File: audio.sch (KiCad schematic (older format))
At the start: 0 parts

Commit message: Add LM386 amp circuits and hierarchy pins.
Add two LM386 amplifier circuit schematics to audio subsystem.
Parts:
- added C? (x2): 100 uF, symbol Device:CP1
- added C? (x6): 0.1 uF, symbol Device:C
- added C? (x2): 1000 uF, symbol Device:CP1
- added C? (x2): 10 uF, symbol Device:CP1
- added C? (x2): 470 pF, symbol Device:C
- added LS? (x2): Speaker, symbol Device:Speaker
- added R? (x2): 10 ohm, symbol Device:R
- added R? (x2): 10k ohm, symbol Device:R
- added RV? (x2): 10k, symbol Device:R_POT_TRIM_US
- added U6, U?: LM386, symbol Amplifier_Audio:LM386
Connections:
- new net: RV?.2, U6.3 (+)
- new net: C?.1, C?.2, U6.5
- new net: R?.1, U6.7 (BYPASS)
- new net: C?.2, LS?.1 (x2)
- new net: C?.1, R?.1 (x2)
- new net: C?.1, R?.2 (x2)
- new net: RV?.2, U?.3 (+)
- new net: C?.1, C?.2, U?.5
- new net: R?.1, U?.7 (BYPASS)
- new net audio-gnd: C?.1, C?.1, C?.1, C?.1, C?.1, C?.1, C?.1, C?.1, C?.2, C?.2, C?.2, C?.2, C?.2, C?.2, C?.2, C?.2, C?.2, C?.2, LS?.2, LS?.2, R?.2, R?.2, RV?.3, RV?.3, U6.2 (-), U6.4 (GND), U6.6 (V+), U?.2 (-), U?.4 (GND), U?.6 (V+)
- new net audio-in-left: RV?.1
- new net audio-in-right: RV?.1
- no-connect marks 0 -> 4

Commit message: Implement Adafruit I2S stereo decoder symbol.
Add stereo decoder to audio subsystem schematic. NOTE: the adafruit
library may be separated out later if necessary. Change hierarchical
schematic pins coming in/out of the audio subsystem.
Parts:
- added U?: UDA1334A, symbol adafruit:UDA1334A
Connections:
- net labels added: agnd, audio-bclk, audio-channel-select, audio-in, bclk, din, wsel
- net labels removed: audio-in-left, audio-in-right
- wire segments 80 -> 91
- no-connect marks 4 -> 11
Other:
- note added: "MUTE might\nbe useful later\nfor software mute"
- moved on the sheet: C?, LS?, R?, RV?, U6, U?

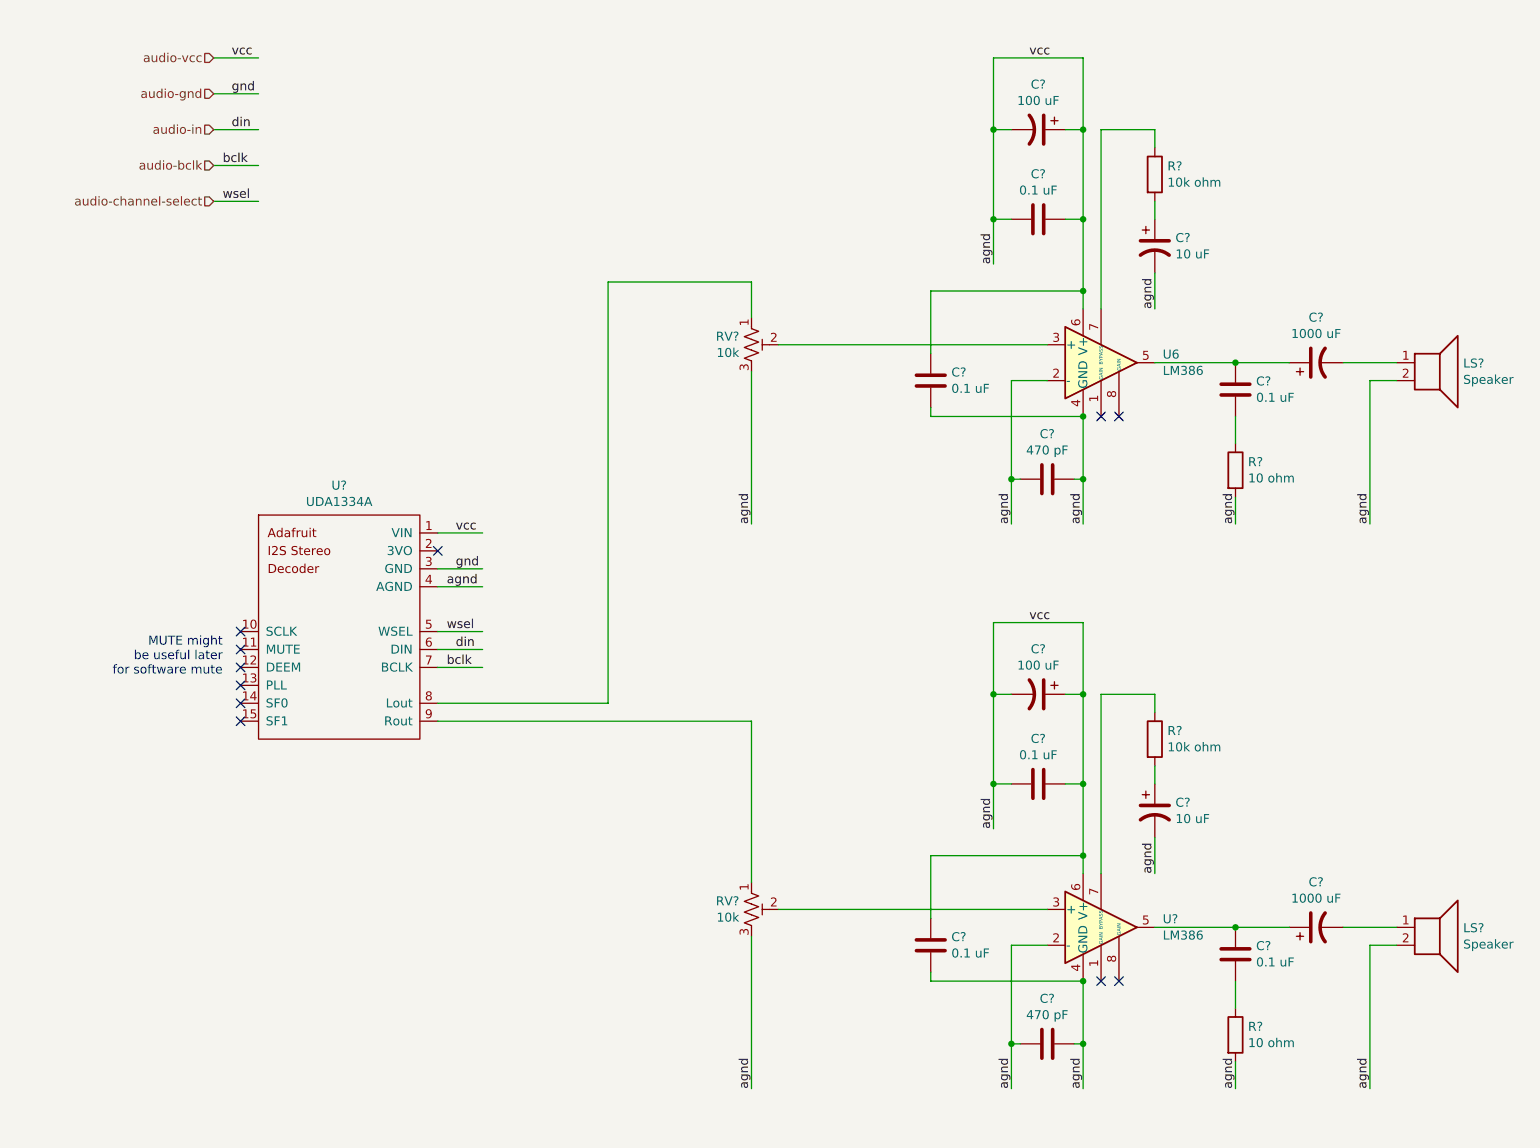
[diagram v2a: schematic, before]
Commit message: Fix power pins to remove ERC warnings.
Add global VCC and GND power pins. Add PWR_FLAG to Arduino VCC and to
audio subsystem power pins to remove ERC warnings.

Add Not Connected to all applicable pins.
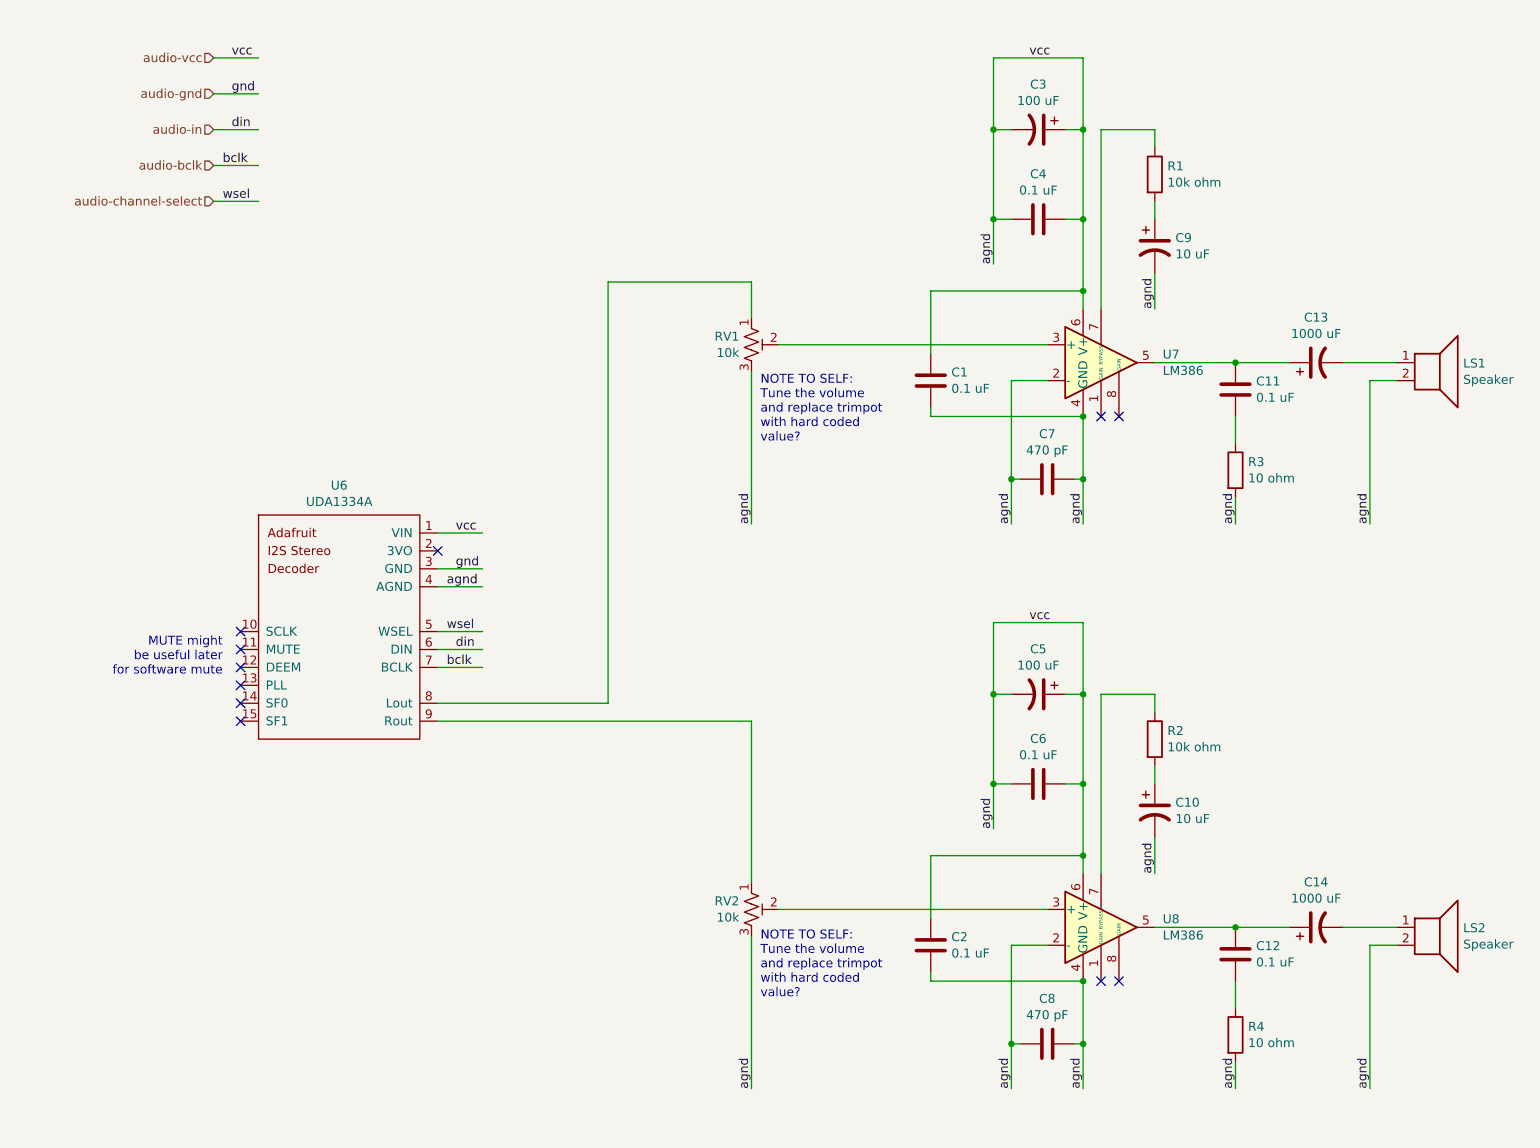
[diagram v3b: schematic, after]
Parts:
- gave numbers to parts that had none: 24
- renumbered U6 to U7
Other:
- note added: "NOTE TO SELF:\nTune the volume\nand replace trimpot\nwith hard coded\nvalue?"
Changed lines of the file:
@@
 $EndDescr
 $Comp
-L Amplifier_Audio:LM386 U6
+L Amplifier_Audio:LM386 U7
 U 1 1 60687AB3
 P 6700 2500
-F 0 "U6" H 7044 2546 50  0000 L CNN
+F 0 "U7" H 7044 2546 50  0000 L CNN
 F 1 "LM386" H 7044 2455 50  0000 L CNN
 F 2 "" H 6800 2600 50  0001 C CNN
@@
 $EndComp
 $Comp
-L Device:Speaker LS?
+L Device:Speaker LS1
 U 1 1 606892D7
 P 8550 2500
-F 0 "LS?" H 8720 2496 50  0000 L CNN
+F 0 "LS1" H 8720 2496 50  0000 L CNN
 F 1 "Speaker" H 8720 2405 50  0000 L CNN
 F 2 "" H 8550 2300 50  0001 C CNN
@@
 agnd
 $Comp
-L Device:C C?
+L Device:C C4
 U 1 1 6068C1D2
 P 6350 1700
-F 0 "C?" V 6098 1700 50  0000 C CNN
+F 0 "C4" V 6098 1700 50  0000 C CNN
 F 1 "0.1 uF" V 6189 1700 50  0000 C CNN
 F 2 "" H 6388 1550 50  0001 C CNN
@@
 $EndComp
 $Comp
-L Device:CP1 C?
+L Device:CP1 C3
 U 1 1 6068BB5D
 P 6350 1200
-F 0 "C?" V 6098 1200 50  0000 C CNN
+F 0 "C3" V 6098 1200 50  0000 C CNN
 F 1 "100 uF" V 6189 1200 50  0000 C CNN
 F 2 "" H 6350 1200 50  0001 C CNN
@@
 NoConn ~ 6800 2800
 $Comp
-L Device:C C?
+L Device:C C11
 U 1 1 6069163A
 P 7450 2650
-F 0 "C?" H 7335 2604 50  0000 R CNN
+F 0 "C11" H 7335 2604 50  0000 R CNN
 F 1 "0.1 uF" H 7335 2695 50  0000 R CNN
 F 2 "" H 7488 2500 50  0001 C CNN
@@
 $EndComp
 $Comp
-L Device:R R?
+L Device:R R3
 U 1 1 60692BCE
 P 7450 3100
-F 0 "R?" H 7520 3146 50  0000 L CNN
+F 0 "R3" H 7520 3146 50  0000 L CNN
 F 1 "10 ohm" H 7520 3055 50  0000 L CNN
 F 2 "" V 7380 3100 50  0001 C CNN
@@
 agnd
 $Comp
-L Device:CP1 C?
+L Device:CP1 C13
 U 1 1 6069368B
 P 7900 2500
-F 0 "C?" V 8152 2500 50  0000 C CNN
+F 0 "C13" V 8152 2500 50  0000 C CNN
 F 1 "1000 uF" V 8061 2500 50  0000 C CNN
 F 2 "" H 7900 2500 50  0001 C CNN
@@
 agnd
 $Comp
-L Device:R R?
+L Device:R R1
 U 1 1 606956EF
 P 7000 1450
-F 0 "R?" H 7070 1496 50  0000 L CNN
+F 0 "R1" H 7070 1496 50  0000 L CNN
 F 1 "10k ohm" H 7070 1405 50  0000 L CNN
 F 2 "" V 6930 1450 50  0001 C CNN
@@
 agnd
 $Comp
-L Device:CP1 C?
+L Device:CP1 C9
 U 1 1 606983F4
 P 7000 1850
-F 0 "C?" H 7115 1896 50  0000 L CNN
+F 0 "C9" H 7115 1896 50  0000 L CNN
 F 1 "10 uF" H 7115 1805 50  0000 L CNN
 F 2 "" H 7000 1850 50  0001 C CNN
@@
 agnd
 $Comp
-L Device:C C?
+L Device:C C7
 U 1 1 606BC090
 P 6400 3150
-F 0 "C?" V 6652 3150 50  0000 C CNN
+F 0 "C7" V 6652 3150 50  0000 C CNN
 F 1 "470 pF" V 6561 3150 50  0000 C CNN
 F 2 "" H 6438 3000 50  0001 C CNN
@@
 	6600 3150 6600 3400
 $Comp
-L Device:C C?
+L Device:C C1
 U 1 1 606BD618
 P 5750 2600
-F 0 "C?" H 5865 2646 50  0000 L CNN
+F 0 "C1" H 5865 2646 50  0000 L CNN
 F 1 "0.1 uF" H 5865 2555 50  0000 L CNN
 F 2 "" H 5788 2450 50  0001 C CNN
@@
 Connection ~ 6600 2800
 $Comp
-L Device:R_POT_TRIM_US RV?
+L Device:R_POT_TRIM_US RV1
 U 1 1 606CBBC0
 P 4750 2400
-F 0 "RV?" H 4682 2446 50  0000 R CNN
+F 0 "RV1" H 4682 2446 50  0000 R CNN
 F 1 "10k" H 4682 2355 50  0000 R CNN
 F 2 "" H 4750 2400 50  0001 C CNN
@@
 	4900 2400 6400 2400
 $Comp
-L Amplifier_Audio:LM386 U?
+L Amplifier_Audio:LM386 U8
 U 1 1 606DD65F
 P 6700 5650
-F 0 "U?" H 7044 5696 50  0000 L CNN
+F 0 "U8" H 7044 5696 50  0000 L CNN
 F 1 "LM386" H 7044 5605 50  0000 L CNN
 F 2 "" H 6800 5750 50  0001 C CNN
@@
 $EndComp
 $Comp
-L Device:Speaker LS?
+L Device:Speaker LS2
 U 1 1 606DD665
 P 8550 5650
-F 0 "LS?" H 8720 5646 50  0000 L CNN
+F 0 "LS2" H 8720 5646 50  0000 L CNN
 F 1 "Speaker" H 8720 5555 50  0000 L CNN
 F 2 "" H 8550 5450 50  0001 C CNN
@@
 agnd
 $Comp
-L Device:C C?
+L Device:C C6
 U 1 1 606DD66D
 P 6350 4850
-F 0 "C?" V 6098 4850 50  0000 C CNN
+F 0 "C6" V 6098 4850 50  0000 C CNN
 F 1 "0.1 uF" V 6189 4850 50  0000 C CNN
 F 2 "" H 6388 4700 50  0001 C CNN
@@
 $EndComp
 $Comp
-L Device:CP1 C?
+L Device:CP1 C5
 U 1 1 606DD673
 P 6350 4350
-F 0 "C?" V 6098 4350 50  0000 C CNN
+F 0 "C5" V 6098 4350 50  0000 C CNN
 F 1 "100 uF" V 6189 4350 50  0000 C CNN
 F 2 "" H 6350 4350 50  0001 C CNN
@@
 NoConn ~ 6800 5950
 $Comp
-L Device:C C?
+L Device:C C12
 U 1 1 606DD689
 P 7450 5800
-F 0 "C?" H 7335 5754 50  0000 R CNN
+F 0 "C12" H 7335 5754 50  0000 R CNN
 F 1 "0.1 uF" H 7335 5845 50  0000 R CNN
 F 2 "" H 7488 5650 50  0001 C CNN
@@
 $EndComp
 $Comp
-L Device:R R?
+L Device:R R4
 U 1 1 606DD68F
 P 7450 6250
-F 0 "R?" H 7520 6296 50  0000 L CNN
+F 0 "R4" H 7520 6296 50  0000 L CNN
 F 1 "10 ohm" H 7520 6205 50  0000 L CNN
 F 2 "" V 7380 6250 50  0001 C CNN
@@
 agnd
 $Comp
-L Device:CP1 C?
+L Device:CP1 C14
 U 1 1 606DD699
 P 7900 5650
-F 0 "C?" V 8152 5650 50  0000 C CNN
+F 0 "C14" V 8152 5650 50  0000 C CNN
 F 1 "1000 uF" V 8061 5650 50  0000 C CNN
 F 2 "" H 7900 5650 50  0001 C CNN
@@
 agnd
 $Comp
-L Device:R R?
+L Device:R R2
 U 1 1 606DD6A5
 P 7000 4600
-F 0 "R?" H 7070 4646 50  0000 L CNN
+F 0 "R2" H 7070 4646 50  0000 L CNN
 F 1 "10k ohm" H 7070 4555 50  0000 L CNN
 F 2 "" V 6930 4600 50  0001 C CNN
@@
 agnd
 $Comp
-L Device:CP1 C?
+L Device:CP1 C10
 U 1 1 606DD6AC
 P 7000 5000
-F 0 "C?" H 7115 5046 50  0000 L CNN
+F 0 "C10" H 7115 5046 50  0000 L CNN
 F 1 "10 uF" H 7115 4955 50  0000 L CNN
 F 2 "" H 7000 5000 50  0001 C CNN
@@
 agnd
 $Comp
-L Device:C C?
+L Device:C C8
 U 1 1 606DD6BC
 P 6400 6300
-F 0 "C?" V 6652 6300 50  0000 C CNN
+F 0 "C8" V 6652 6300 50  0000 C CNN
 F 1 "470 pF" V 6561 6300 50  0000 C CNN
 F 2 "" H 6438 6150 50  0001 C CNN
@@
 	6600 6300 6600 6550
 $Comp
-L Device:C C?
+L Device:C C2
 U 1 1 606DD6C8
 P 5750 5750
-F 0 "C?" H 5865 5796 50  0000 L CNN
+F 0 "C2" H 5865 5796 50  0000 L CNN
 F 1 "0.1 uF" H 5865 5705 50  0000 L CNN
 F 2 "" H 5788 5600 50  0001 C CNN
@@
 Connection ~ 6600 5950
 $Comp
-L Device:R_POT_TRIM_US RV?
+L Device:R_POT_TRIM_US RV2
 U 1 1 606DD6D6
 P 4750 5550
-F 0 "RV?" H 4682 5596 50  0000 R CNN
+F 0 "RV2" H 4682 5596 50  0000 R CNN
 F 1 "10k" H 4682 5505 50  0000 R CNN
 F 2 "" H 4750 5550 50  0001 C CNN
@@
 	4900 5550 6400 5550
 $Comp
-L adafruit:UDA1334A U?
+L adafruit:UDA1334A U6
 U 1 1 6067F8B5
 P 2450 4000
-F 0 "U?" H 2450 4815 50  0000 C CNN
+F 0 "U6" H 2450 4815 50  0000 C CNN
 F 1 "UDA1334A" H 2450 4724 50  0000 C CNN
 F 2 "" H 2250 4700 50  0001 C CNN
@@
 Text HLabel 1750 1600 0    50   Input ~ 0
 audio-channel-select
-Wire Wire Line
-	1750 1600 2000 1600
 Text Label 1800 1600 0    50   ~ 0
 wsel
-Wire Wire Line
-	3000 4000 3250 4000
 Wire Wire Line
 	3000 4200 3250 4200
@@
 Text Label 3050 4200 0    50   ~ 0
 bclk
+Text Notes 4800 2950 0    50   ~ 0
+NOTE TO SELF:\nTune the volume\nand replace trimpot\nwith hard coded\nvalue?
+Text Notes 4800 6050 0    50   ~ 0
+NOTE TO SELF:\nTune the volume\nand replace trimpot\nwith hard coded\nvalue?
+Wire Wire Line
+	1750 1600 2000 1600
+Wire Wire Line
+	3000 4000 3250 4000
 $EndSCHEMATC

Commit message: Move most PWR_FLAGs into corner and use GNDA.
Use GNDA power pin in the audio subsystem instead of "agnd" sheet label.
Re-examine application of PWR_FLAGS after reading the wiki page.

Change the symbol for thumbstick in controller subsystem to reflect that
it's actually the FPC connector and not actually the thumbstick module.
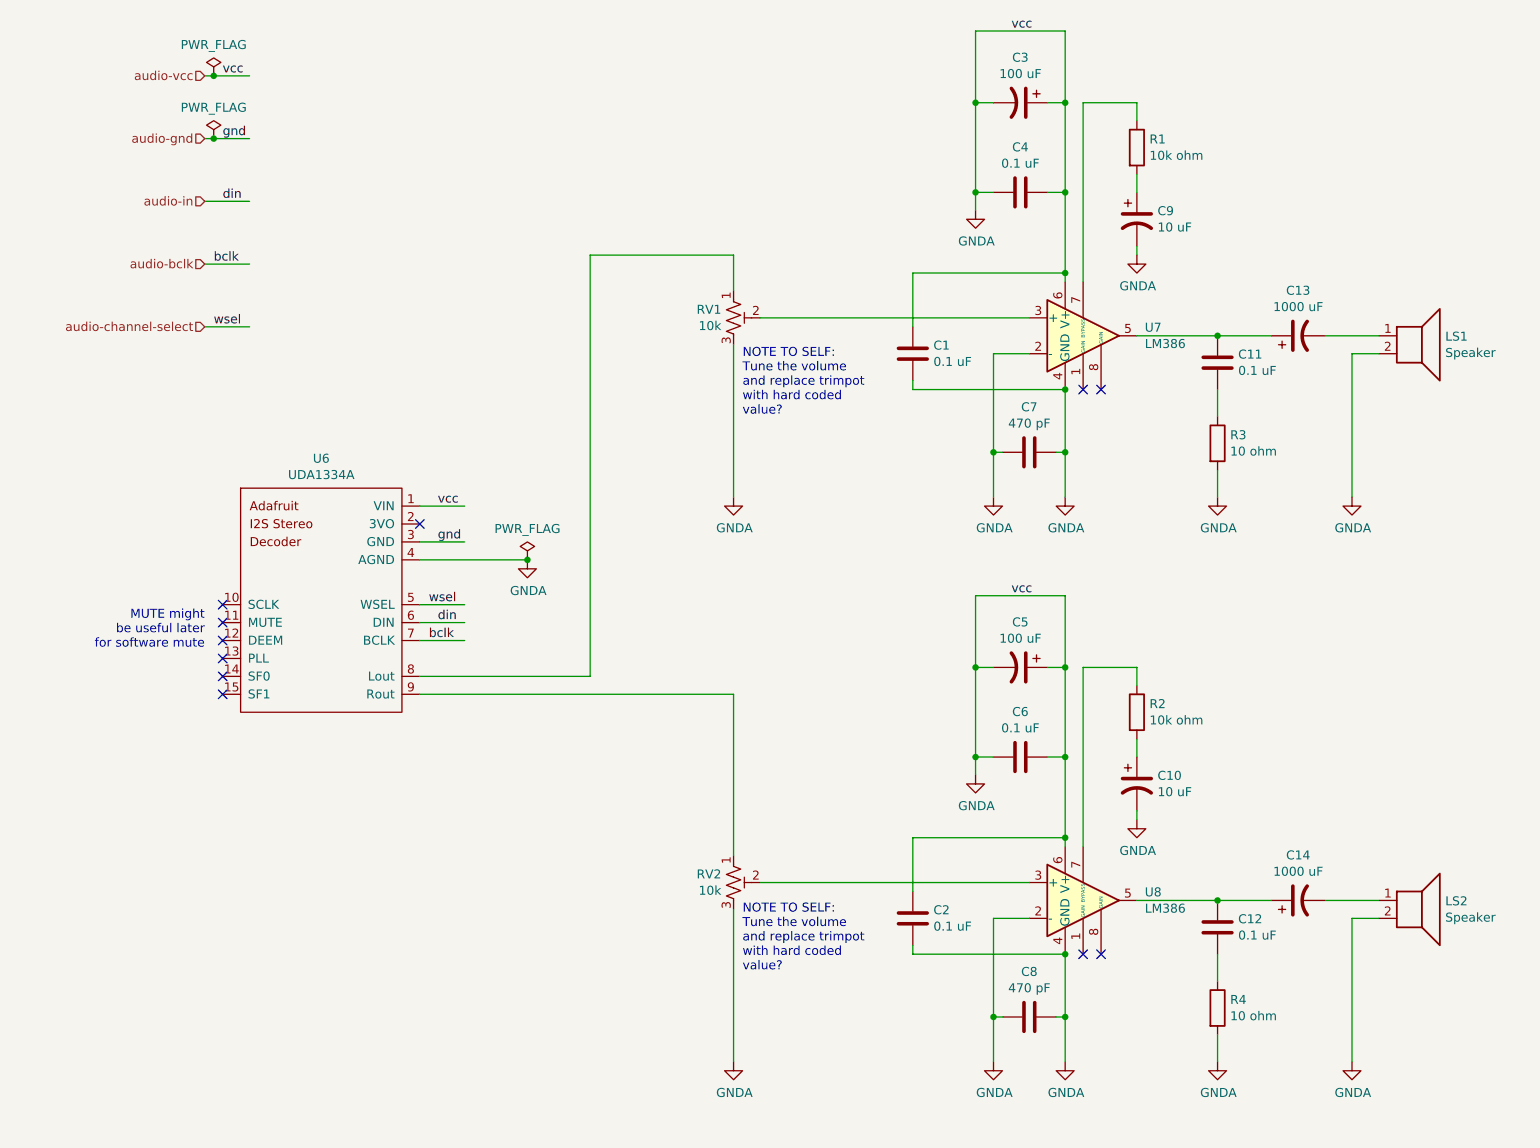
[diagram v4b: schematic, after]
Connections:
- net labels added: GNDA
- net labels removed: agnd
- wire segments 91 -> 93
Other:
- moved on the sheet: C1, C10, C11, C12, C13, C14, C2, C3, C4, C5, C6, C7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
